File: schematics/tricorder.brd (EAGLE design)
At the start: 90.2 x 73.7 mm, 75 parts, among them IC1 EADOGM128, U1 V_REG_LDOSMD, U2 CY8C5XXX, U3 M05X2-0.05-SMD, U7 MICROUSB

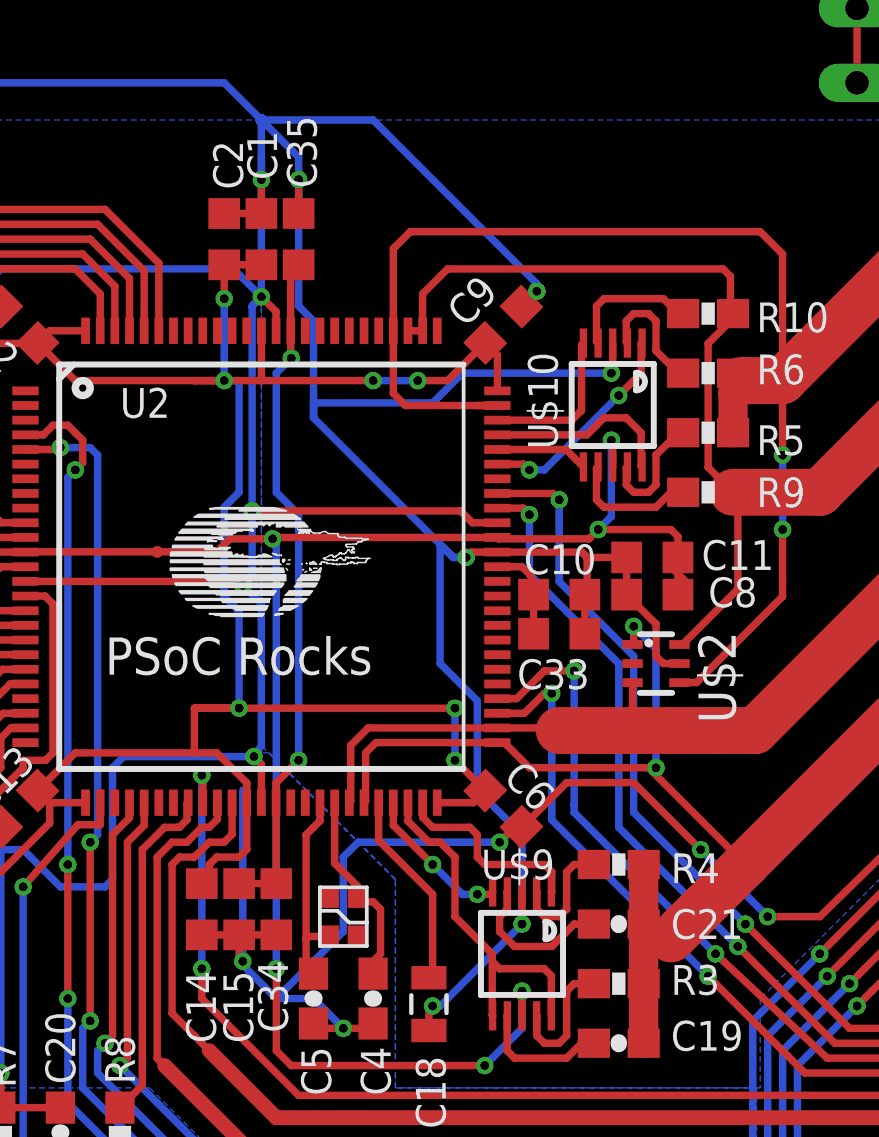
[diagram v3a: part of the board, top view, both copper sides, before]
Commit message: Fixed LCD handling in firmware
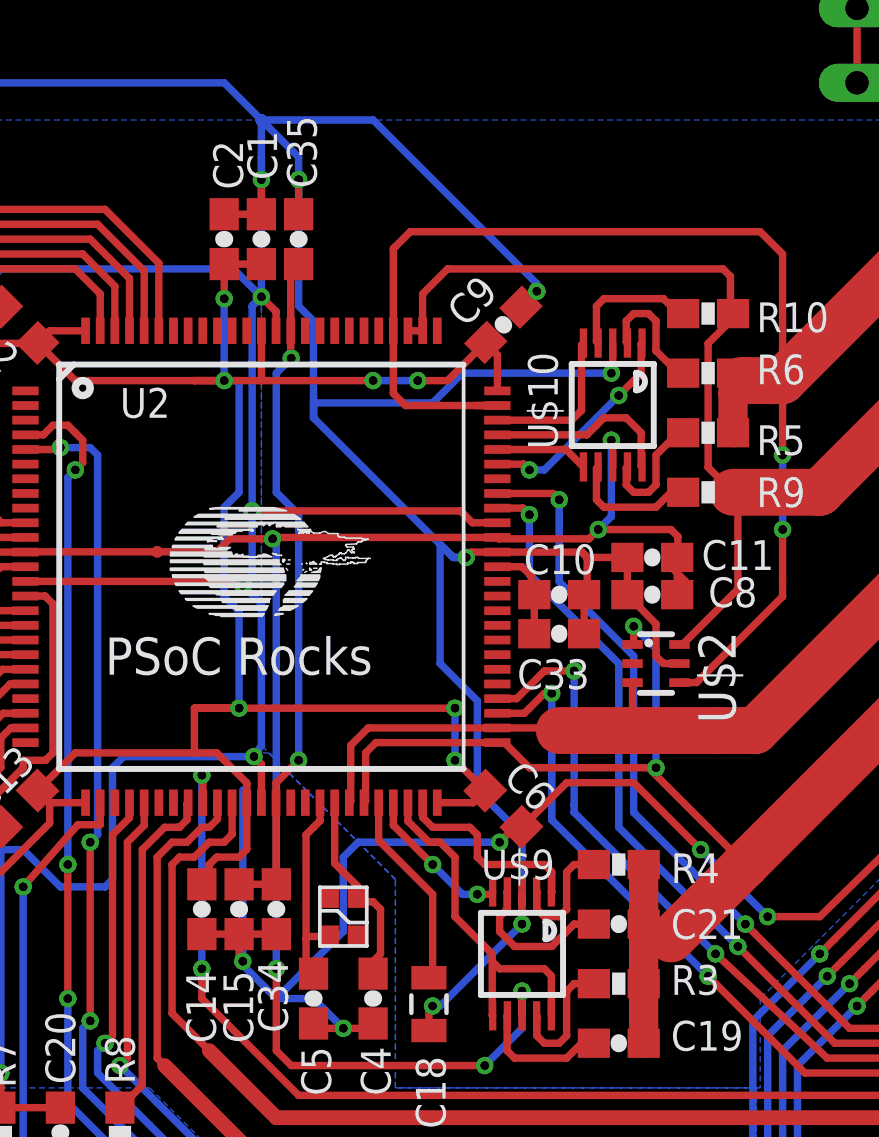
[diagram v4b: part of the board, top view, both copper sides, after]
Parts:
- C1, C10, C11, C14, C15, C2, C33, C34, C35, C8, C9: device resistor:C0603K -> SparkFun-Passives:0603-CAP
